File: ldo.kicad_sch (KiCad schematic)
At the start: 0 parts

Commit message: ldo and buck updated, footprints added
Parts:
- added C23, C24: C_Polarized, symbol Device:C_Polarized
- added Q6: NMOS, Package_TO_SOT_THT:TO-220-3_Vertical, symbol Simulation_SPICE:NMOS
- added R36, R37, R38, R39: R, symbol Device:R
- added U19: OPA705PA, footprints10:P8, symbol opa705:OPA705PA
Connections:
- new net: C23.2, R36.2, R39.1, U19.2 (IN-)
- new net: Q6.1 (G), R37.1
- new net: R37.2, U19.6 (OUT)
- new net +3.3V: C23.1, C24.1, Q6.3 (S), R36.1, R38.1
- new net +3.5V: Q6.2 (D)
- new net GND: C24.2, R38.2, R39.2
- new net volt_ref: U19.3 (IN+)

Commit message: schematic cleanup
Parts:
- added R40, R41: 0, Resistor_SMD:R_0805_2012Metric, symbol Device:R
- C23, C24: footprint (none) -> Capacitor_SMD:C_0805_2012Metric; symbol Device:C_Polarized -> Device:C
- R36, R37, R38, R39: footprint (none) -> Resistor_SMD:R_0805_2012Metric
- U19: footprint footprints10:P8 -> footprints:P8
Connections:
- net +3.5V: now also R40.1; no longer Q6.2 (D)
- net GND: now also U19.4 (V-)
- net PWR_IN: now reaches U19.7 (V+)
- new net: Q6.2 (D), R40.2, R41.2
- new net +9V: R41.1
- no-connect marks 0 -> 3
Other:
- moved on the sheet: Q6, R36, R37, R38, R39, U19

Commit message: pcb layout
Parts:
- added C45: C_Polarized, Capacitor_SMD:C_0805_2012Metric, symbol Device:C
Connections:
- net GND: now also C45.2
- net PWR_IN: now also C45.1
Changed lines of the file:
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@@
+	)
+	(junction
+		(at 135.255 41.91)
+		(diameter 0)
+		(color 0 0 0 0)
 	)
 	(junction
@@
 	(wire
 		(pts
+			(xy 135.255 41.91) (xy 133.35 41.91)
+		)
+		(stroke
+			(width 0)
+			(type default)
+		)
+	)
+	(wire
+		(pts
 			(xy 71.755 60.96) (xy 76.2 60.96)
 		)
@@
 	(wire
 		(pts
+			(xy 133.35 58.42) (xy 132.08 58.42)
+		)
+		(stroke
+			(width 0)
+			(type default)
+		)
+	)
+	(wire
+		(pts
 			(xy 128.905 104.775) (xy 128.905 101.6)
 		)
@@
 	(wire
 		(pts
+			(xy 133.35 41.91) (xy 133.35 58.42)
+		)
+		(stroke
+			(width 0)
+			(type default)
+		)
+	)
+	(wire
+		(pts
 			(xy 59.69 86.36) (xy 95.25 86.36)
 		)
@@
 		(pts
 			(xy 59.69 58.42) (xy 76.2 58.42)
+		)
+		(stroke
+			(width 0)
+			(type default)
+		)
+	)
+	(wire
+		(pts
+			(xy 136.525 41.91) (xy 135.255 41.91)
 		)
 		(stroke
@@
 	(hierarchical_label "PWR_IN"
 		(shape input)
-		(at 132.08 58.42 0)
+		(at 136.525 41.91 0)
 		(effects
 			(font
@@
 	)
 	(symbol
+		(lib_id "Device:C")
+		(at 135.255 45.72 0)
+		(unit 1)
+		(exclude_from_sim no)
+		(in_bom yes)
+		(on_board yes)
+		(dnp no)
+		(property "Reference" "C45"
+			(at 138.43 43.5609 0)
+			(effects
+				(font
+					(size 1.27 1.27)
+				)
+				(justify left)
+			)
+		)
+		(property "Value" "C_Polarized"
+			(at 138.43 46.1009 0)
+			(effects
+				(font
+					(size 1.27 1.27)
+				)
+				(justify left)
+			)
+		)
+		(property "Footprint" "Capacitor_SMD:C_0805_2012Metric"
+			(at 136.2202 49.53 0)
+			(effects
+				(font
+					(size 1.27 1.27)
+				)
+				(hide yes)
+			)
+		)
+		(property "Datasheet" "~"
+			(at 135.255 45.72 0)
+			(effects
+				(font
+					(size 1.27 1.27)
+				)
+				(hide yes)
+			)
+		)
+		(property "Description" "Unpolarized capacitor"
+			(at 135.255 45.72 0)
+			(effects
+				(font
+					(size 1.27 1.27)
+				)
+				(hide yes)
+			)
+		)
+		(pin "1"
+		)
+		(pin "2"
+		)
+		(instances
+			(project "ee115-capstone"
+				(path "/80dfed98-7d85-4c9a-bb85-182165e7352f/d0fb3630-b484-4405-bb3b-b4246eeb0dac"
+					(reference "C45")
+					(unit 1)
+				)
+			)
+		)
+	)
+	(symbol
 		(lib_id "Device:R")
 		(at 137.795 60.96 270)
@@
 					(unit 1)
 				)
+			)
+		)
+	)
+	(symbol
+		(lib_id "power:GND")
+		(at 135.255 49.53 0)
+		(unit 1)
+		(exclude_from_sim no)
+		(in_bom yes)
+		(on_board yes)
+		(dnp no)
+		(fields_autoplaced yes)
+		(property "Reference" "#PWR0114"
+			(at 135.255 55.88 0)
+			(effects
+				(font
+					(size 1.27 1.27)
+				)
+				(hide yes)
+			)
+		)
+		(property "Value" "GND"
+			(at 135.255 54.61 0)
+			(effects
+				(font
+					(size 1.27 1.27)
+				)
+			)
+		)
+		(property "Footprint" ""
+			(at 135.255 49.53 0)
+			(effects
+				(font
+					(size 1.27 1.27)
+				)
+				(hide yes)
+			)
+		)
+		(property "Datasheet" ""
+			(at 135.255 49.53 0)
+			(effects
+				(font
+					(size 1.27 1.27)
+				)
+				(hide yes)
+			)
+		)
+		(property "Description" "Power symbol creates a global label with name \"GND\" , ground"
+			(at 135.255 49.53 0)
+			(effects
+				(font
+					(size 1.27 1.27)
+				)
+				(hide yes)
+			)
+		)
+		(pin "1"
+		)
+		(instances
+			(project "ee115-capstone"
+				(path "/80dfed98-7d85-4c9a-bb85-182165e7352f/d0fb3630-b484-4405-bb3b-b4246eeb0dac"
+					(reference "#PWR0114")
+					(unit 1)
+				)

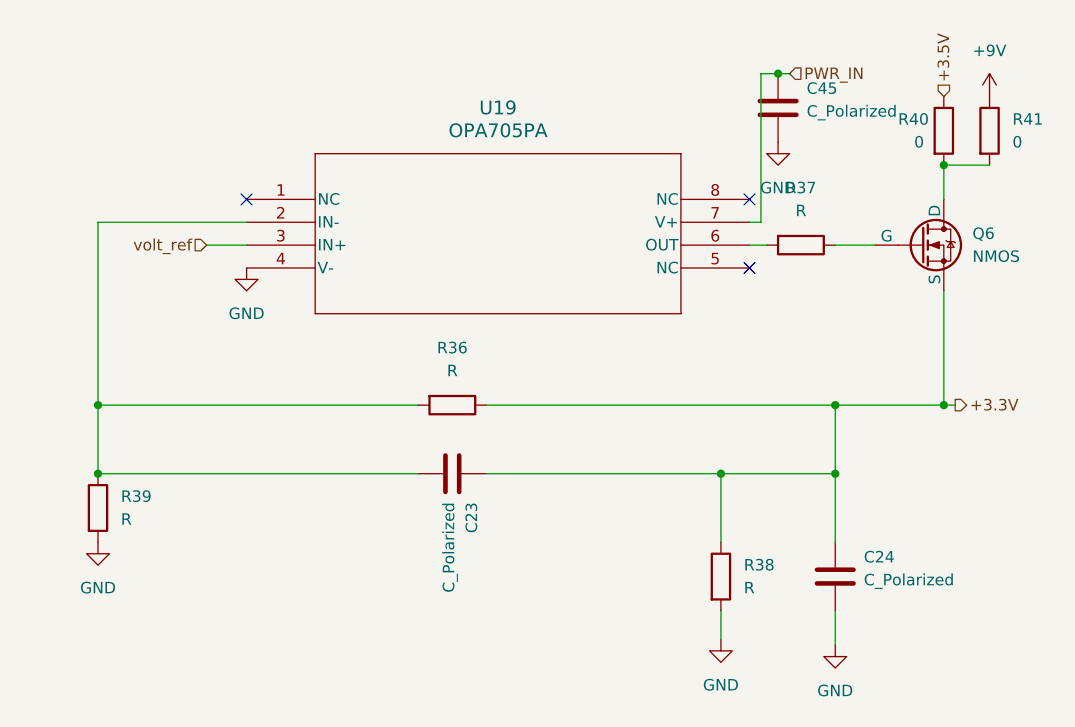
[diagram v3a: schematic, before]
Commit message: pcb layout component placement 90% done
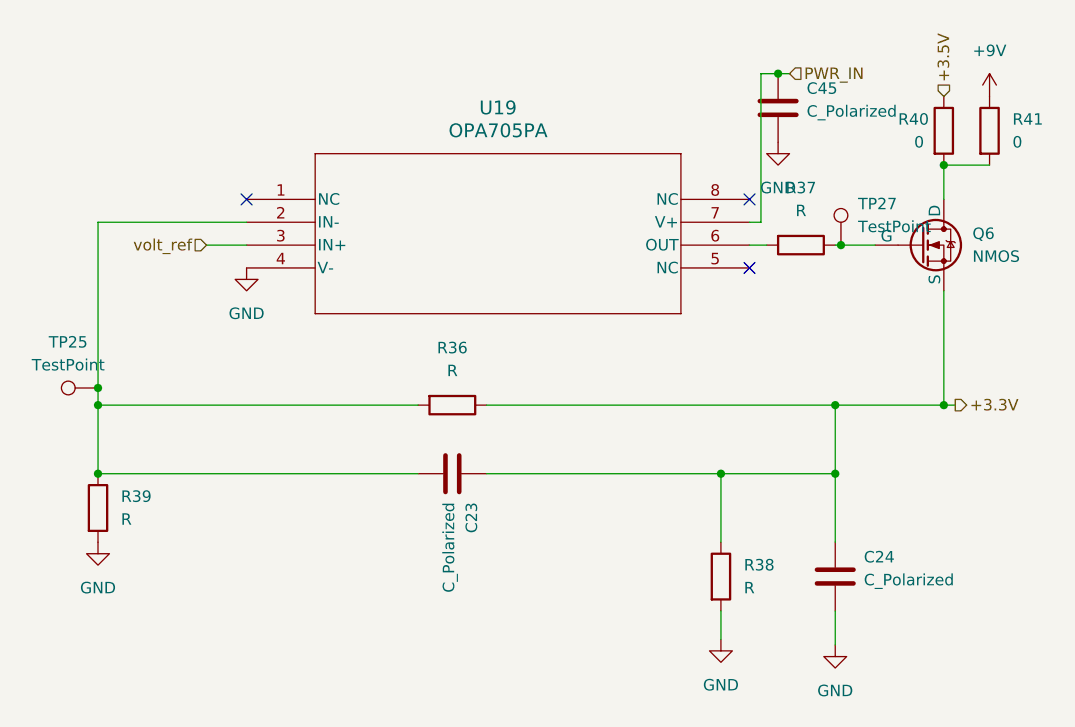
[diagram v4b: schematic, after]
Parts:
- added TP25, TP27: TestPoint, TestPoint:TestPoint_Plated_Hole_D2.0mm, symbol Connector:TestPoint
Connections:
- net at C23.2, R36.2, R39.1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: now also TP25.1
- net at Q6.1 (G), R37.1: now also TP27.1
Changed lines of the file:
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@@
 	(paper "A4")
+	(junction
+		(at 59.69 76.835)
+		(diameter 0)
+		(color 0 0 0 0)
+	)
 	(junction
 		(at 59.69 78.74)
@@
 	)
 	(junction
+		(at 142.24 60.96)
+		(diameter 0)
+		(color 0 0 0 0)
+	)
+	(junction
 		(at 141.605 86.36)
 		(diameter 0)
@@
 	(wire
 		(pts
+			(xy 142.24 60.96) (xy 146.05 60.96)
+		)
+		(stroke
+			(width 0)
+			(type default)
+		)
+	)
+	(wire
+		(pts
 			(xy 135.255 41.91) (xy 133.35 41.91)
 		)
@@
 	(wire
 		(pts
-			(xy 59.69 58.42) (xy 59.69 78.74)
+			(xy 59.69 76.835) (xy 59.69 78.74)
+		)
+		(stroke
+			(width 0)
+			(type default)
+		)
+	)
+	(wire
+		(pts
+			(xy 59.69 58.42) (xy 59.69 76.835)
 		)
 		(stroke
@@
 	(wire
 		(pts
-			(xy 141.605 60.96) (xy 146.05 60.96)
+			(xy 141.605 60.96) (xy 142.24 60.96)
 		)
 		(stroke
@@
 	)
 	(symbol
+		(lib_id "Connector:TestPoint")
+		(at 59.69 76.835 90)
+		(unit 1)
+		(exclude_from_sim no)
+		(in_bom yes)
+		(on_board yes)
+		(dnp no)
+		(fields_autoplaced yes)
+		(property "Reference" "TP25"
+			(at 56.388 71.755 90)
+			(effects
+				(font
+					(size 1.27 1.27)
+				)
+			)
+		)
+		(property "Value" "TestPoint"
+			(at 56.388 74.295 90)
+			(effects
+				(font
+					(size 1.27 1.27)
+				)
+			)
+		)
+		(property "Footprint" "TestPoint:TestPoint_Plated_Hole_D2.0mm"
+			(at 59.69 71.755 0)
+			(effects
+				(font
+					(size 1.27 1.27)
+				)
+				(hide yes)
+			)
+		)
+		(property "Datasheet" "~"
+			(at 59.69 71.755 0)
+			(effects
+				(font
+					(size 1.27 1.27)
+				)
+				(hide yes)
+			)
+		)
+		(property "Description" "test point"
+			(at 59.69 76.835 0)
+			(effects
+				(font
+					(size 1.27 1.27)
+				)
+				(hide yes)
+			)
+		)
+		(pin "1"
+		)
+		(instances
+			(project "ee115-capstone"
+				(path "/80dfed98-7d85-4c9a-bb85-182165e7352f/d0fb3630-b484-4405-bb3b-b4246eeb0dac"
+					(reference "TP25")
+					(unit 1)
+				)
+			)
+		)
+	)
+	(symbol
 		(lib_id "Device:R")
 		(at 153.67 48.26 0)
@@
 					(unit 1)
 				)
+			)
+		)
+	)
+	(symbol
+		(lib_id "Connector:TestPoint")
+		(at 142.24 60.96 0)
+		(unit 1)
+		(exclude_from_sim no)
+		(in_bom yes)
+		(on_board yes)
+		(dnp no)
+		(fields_autoplaced yes)
+		(property "Reference" "TP27"
+			(at 144.145 56.3879 0)
+			(effects
+				(font
+					(size 1.27 1.27)
+				)
+				(justify left)
+			)
+		)
+		(property "Value" "TestPoint"
+			(at 144.145 58.9279 0)
+			(effects
+				(font
+					(size 1.27 1.27)
+				)
+				(justify left)
+			)
+		)
+		(property "Footprint" "TestPoint:TestPoint_Plated_Hole_D2.0mm"
+			(at 147.32 60.96 0)
+			(effects
+				(font
+					(size 1.27 1.27)
+				)
+				(hide yes)
+			)
+		)
+		(property "Datasheet" "~"
+			(at 147.32 60.96 0)
+			(effects
+				(font
+					(size 1.27 1.27)
+				)
+				(hide yes)
+			)
+		)
+		(property "Description" "test point"
+			(at 142.24 60.96 0)
+			(effects
+				(font
+					(size 1.27 1.27)
+				)
+				(hide yes)
+			)
+		)
+		(pin "1"
+		)
+		(instances
+			(project "ee115-capstone"
+				(path "/80dfed98-7d85-4c9a-bb85-182165e7352f/d0fb3630-b484-4405-bb3b-b4246eeb0dac"
+					(reference "TP27")
+					(unit 1)
+				)

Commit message: pcb layout draft
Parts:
- C23, C24, C45: footprint Capacitor_SMD:C_0805_2012Metric -> footprints_pretty:0805_cap_nosilk
- R36, R37, R38, R39, R40, R41: footprint Resistor_SMD:R_0805_2012Metric -> footprints_pretty:res_0805_nosilk
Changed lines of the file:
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@@
 			)
 		)
-		(property "Footprint" "Resistor_SMD:R_0805_2012Metric"
+		(property "Footprint" "footprints_pretty:res_0805_nosilk"
 			(at 127.127 97.79 90)
 			(effects
@@
 			)
 		)
-		(property "Footprint" "Resistor_SMD:R_0805_2012Metric"
+		(property "Footprint" "footprints_pretty:res_0805_nosilk"
 			(at 156.972 48.26 90)
 			(effects
@@
 			)
 		)
-		(property "Footprint" "Resistor_SMD:R_0805_2012Metric"
+		(property "Footprint" "footprints_pretty:res_0805_nosilk"
 			(at 151.892 48.26 90)
 			(effects
@@
 			)
 		)
-		(property "Footprint" "Capacitor_SMD:C_0805_2012Metric"
+		(property "Footprint" "footprints_pretty:0805_cap_nosilk"
 			(at 95.25 87.3252 0)
 			(effects
@@
 			)
 		)
-		(property "Footprint" "Capacitor_SMD:C_0805_2012Metric"
+		(property "Footprint" "footprints_pretty:0805_cap_nosilk"
 			(at 136.2202 49.53 0)
 			(effects
@@
 			)
 		)
-		(property "Footprint" "Resistor_SMD:R_0805_2012Metric"
+		(property "Footprint" "footprints_pretty:res_0805_nosilk"
 			(at 137.795 59.182 90)
 			(effects
@@
 			)
 		)
-		(property "Footprint" "Resistor_SMD:R_0805_2012Metric"
+		(property "Footprint" "footprints_pretty:res_0805_nosilk"
 			(at 57.912 90.17 90)
 			(effects
@@
 			)
 		)
-		(property "Footprint" "Capacitor_SMD:C_0805_2012Metric"
+		(property "Footprint" "footprints_pretty:0805_cap_nosilk"
 			(at 142.5702 101.6 0)
 			(effects
@@
 			)
 		)
-		(property "Footprint" "Resistor_SMD:R_0805_2012Metric"
+		(property "Footprint" "footprints_pretty:res_0805_nosilk"
 			(at 99.06 76.962 90)
 			(effects

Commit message: changed values
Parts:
- C23: value C_Polarized -> 100pF
- C24: value C_Polarized -> 22uF
- Q6: value NMOS -> IRLZ44N
- R36: value R -> 18.7K
- R37: value R -> 100
- R38: value R -> Load
- R39: value R -> 10k
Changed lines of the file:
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@@
 			)
 		)
-		(property "Value" "R"
+		(property "Value" "Load"
 			(at 131.445 99.0599 0)
 			(effects
@@
 			)
 		)
-		(property "Value" "C_Polarized"
+		(property "Value" "100pF"
 			(at 98.6791 89.535 0)
 			(effects
@@
 			)
 		)
-		(property "Value" "NMOS"
+		(property "Value" "IRLZ44N"
 			(at 156.845 62.2299 0)
 			(effects
@@
 			)
 		)
-		(property "Value" "R"
+		(property "Value" "100"
 			(at 137.795 57.15 90)
 			(effects
@@
 			)
 		)
-		(property "Value" "R"
+		(property "Value" "10k"
 			(at 62.23 91.4399 0)
 			(effects
@@
 			)
 		)
-		(property "Value" "C_Polarized"
+		(property "Value" "22uF"
 			(at 144.78 98.1709 0)
 			(effects
@@
 			)
 		)
-		(property "Value" "R"
+		(property "Value" "18.7K"
 			(at 99.06 74.93 90)
 			(effects
